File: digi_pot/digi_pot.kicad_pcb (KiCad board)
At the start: 2 copper layers, 30 x 30 mm, 22 parts, among them J1 Conn_01x08_Male, J2 Conn_01x06_Male, J3 Conn_01x03_Male, J4 Conn_01x03_Male, J5 Conn_01x06_Male, SW1 Rotary_Encoder, U1 ATmega328P-AU, U2 MCP42050

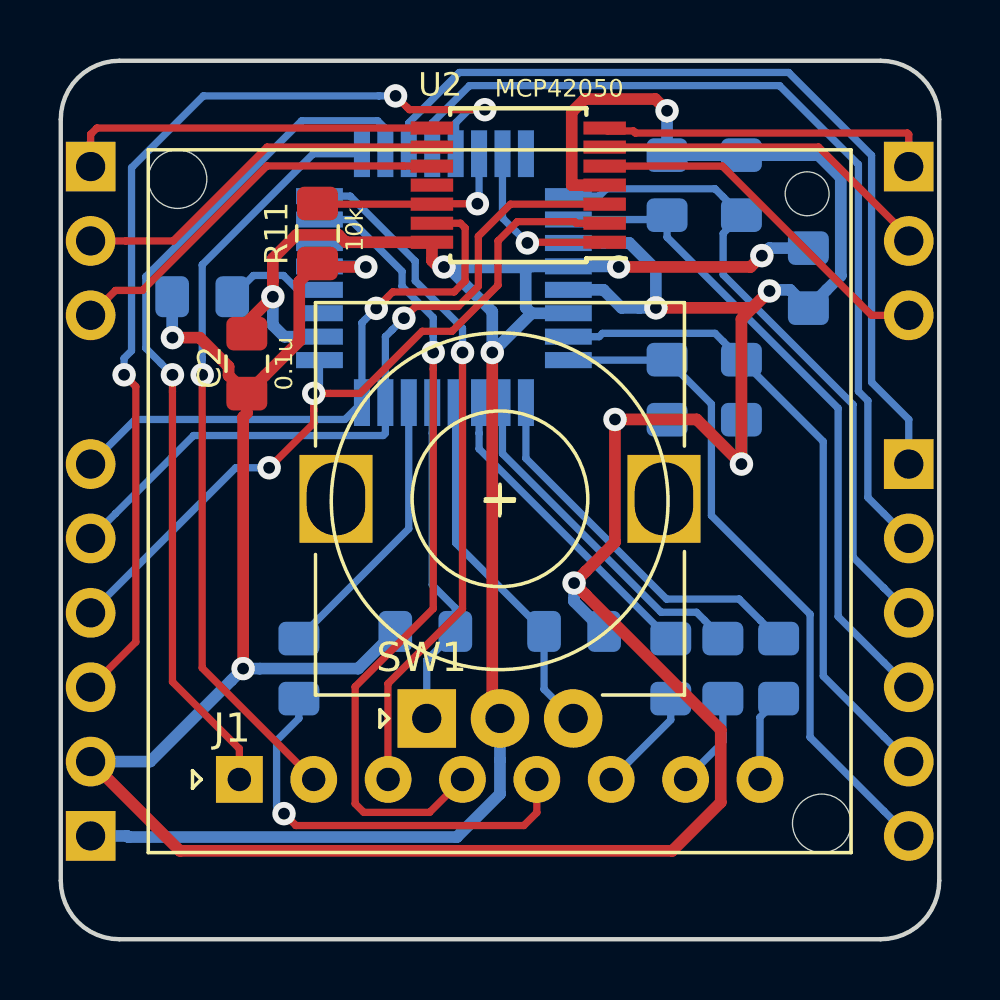
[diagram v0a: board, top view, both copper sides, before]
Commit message: Switching to AD5262 digital pot.
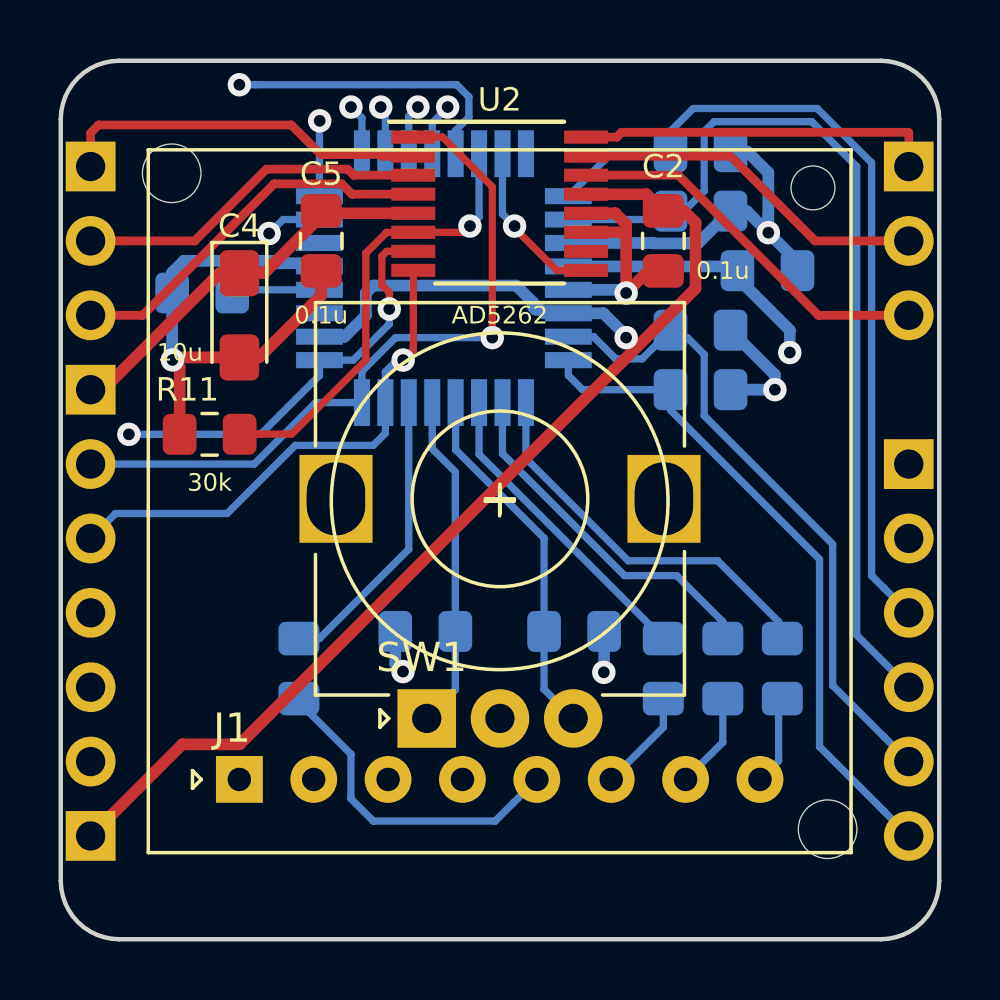
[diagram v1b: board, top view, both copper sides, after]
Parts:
- added C4: 10u, Capacitor_Tantalum_SMD:CP_EIA-3216-18_Kemet-A_Pad1.58x1.35mm_HandSolder, F.Cu at (139.7, 86.4)
- added C5: 0.1u, Capacitor_SMD:C_0805_2012Metric_Pad1.15x1.40mm_HandSolder, F.Cu at (142.5, 83.8)
- added J6: Conn_01x01_Male, Connector_PinHeader_2.54mm:PinHeader_1x01_P2.54mm_Vertical, B.Cu at (134.6, 88.9)
- R10, R11, R5, R6, R7, R8, R9: value 10k -> 30k
- U2: value MCP42050 -> AD5262; footprint Package_SO:TSSOP-14_4.4x5mm_P0.65mm -> Package_SO:TSSOP-16_4.4x5mm_P0.65mm
- moved C2 14.8 mm to (154.2, 83.8)
- moved R11 7.78 mm to (138.7, 90.4), turned to 0 degrees
- moved R9 2.47 mm to (155.4, 86.9), turned to 180 degrees
- moved R7 1.81 mm to (155.4, 80.8), turned to 180 degrees
- moved R8 1.45 mm to (155.4, 82.8), turned to 180 degrees
- moved C1 1.42 mm to (157.7, 84.8), turned to 0 degrees
- moved R10 1.14 mm to (155.4, 88.9), turned to 180 degrees
- moved U2 0.90 mm to (148.6, 82.5), turned to 0 degrees
- moved R2 0.25 mm to (154.2, 98.4)
- moved C3 0.13 mm to (138.4, 85.6)
- moved R4 0.13 mm to (158.2, 98.4)
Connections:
- U2 pad 1: MCP_CS -> MISO
- U2 pad 10: Net-(J3-Pad3) -> Net-(U2-Pad10)
- U2 pad 11: Net-(U2-Pad11) -> GND
- U2 pad 12: MCP_SHDN -> GND
- U2 pad 13: MISO -> +5V
- U2 pad 14: +5V -> Net-(J4-Pad3)
- U2 pad 2: SCK -> Net-(J3-Pad1)
- U2 pad 3: MOSI -> Net-(J3-Pad2)
- U2 pad 4: GND -> Net-(J3-Pad3)
- U2 pad 5: Net-(J4-Pad3) -> +9V
- U2 pad 6: Net-(J4-Pad2) -> MCP_SHDN
- U2 pad 7: Net-(J4-Pad1) -> SCK
- U2 pad 8: Net-(J3-Pad1) -> MOSI
- U2 pad 9: Net-(J3-Pad2) -> MCP_CS
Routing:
- net +5V: track 63.6 -> 105.3 mm, vias 5 -> 2
- net GND: track 124.6 -> 107.0 mm, vias 9 -> 6
- net +9V: track 0.00 -> 13.7 mm
- net A1: track 23.0 -> 31.6 mm
- net MCP_SHDN: track 7.21 -> 15.6 mm
- net MOSI: track 25.2 -> 17.6 mm
- net A0: track 22.9 -> 28.7 mm
- net SCL: track 30.7 -> 25.6 mm, vias 0 -> 1
- net SCK: track 25.8 -> 21.0 mm
- net MISO: track 20.0 -> 24.7 mm
- net SDA: track 29.8 -> 25.4 mm, vias 0 -> 1
- net Net-(J1-Pad5): track 14.8 -> 11.4 mm, vias 1 -> 0
- net LED3: track 23.6 -> 26.2 mm
- net LED2: track 26.4 -> 28.3 mm
- net RST: track 34.2 -> 32.8 mm, vias 3 -> 1
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- added copper zone on In1.Cu, net GND
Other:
- copper layers 2 -> 4
- net class Medium added: clearance 0.2, trace_width 0.3, via_dia 0.8, via_drill 0.4
- board text added: "+9V"
- board text added: "2020.02.12"
- board text removed: "2019.09.23"

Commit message: Using standard Atmega328 symbol.
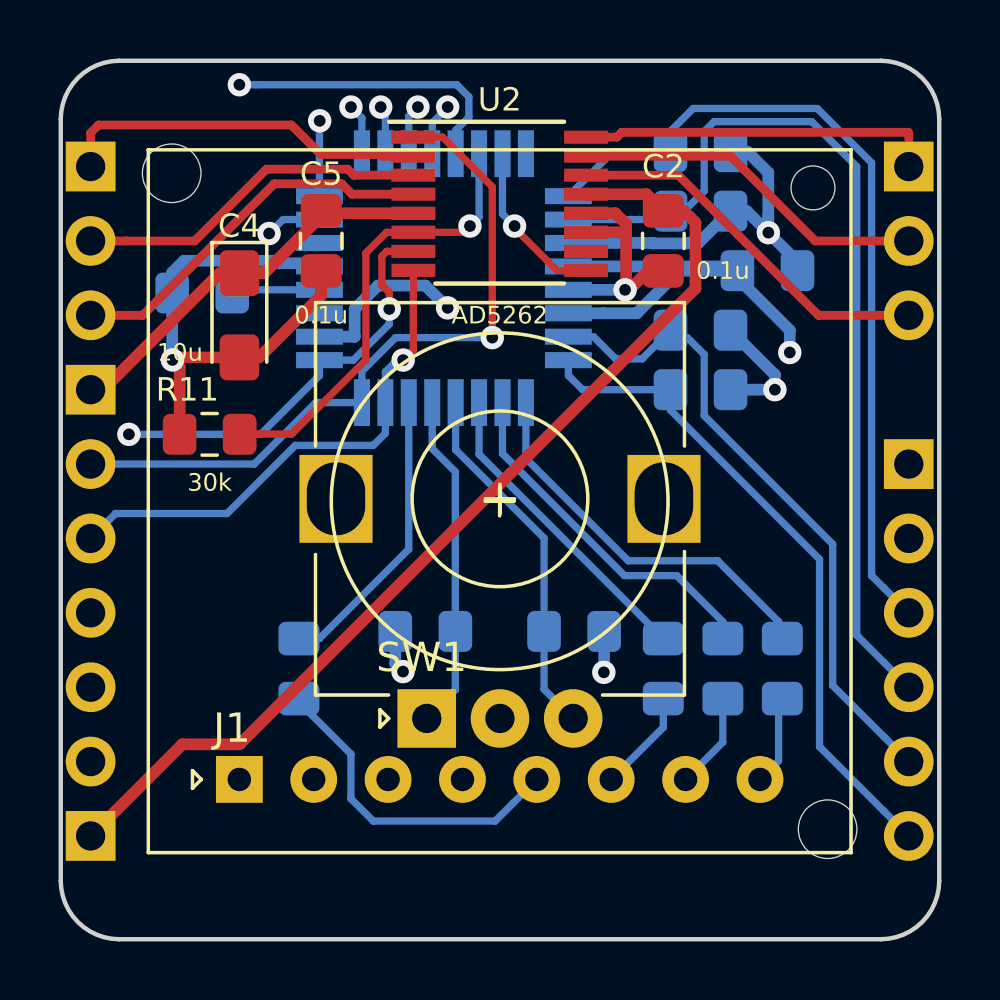
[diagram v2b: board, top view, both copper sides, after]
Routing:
- net +5V: track 105.3 -> 111.0 mm
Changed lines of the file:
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@@
     (thickness 1.6)
     (drawings 26)
-    (tracks 363)
+    (tracks 359)
     (zones 0)
     (modules 25)
@@
     (tags "QFP 0.8")
     (attr smd)
-    (fp_text reference U1 (at -0.127 5.842 180) (layer B.SilkS)
+    (fp_text reference U1 (at 0 6.05) (layer B.SilkS)
       (effects (font (size 0.8 0.8) (thickness 0.1)) (justify mirror))
     )
-    (fp_text value ATmega328P-AU (at -1.651 -5.842 180) (layer B.SilkS)
+    (fp_text value ATmega328P-AU (at 0 -6.05) (layer B.SilkS)
       (effects (font (size 0.6 0.6) (thickness 0.1)) (justify mirror))
     )
-    (fp_text user %R (at 0 0 180) (layer B.Fab)
+    (fp_text user %R (at 0 0) (layer B.Fab)
       (effects (font (size 1 1) (thickness 0.15)) (justify mirror))
     )
@@
   (segment (start 157.048 80.772) (end 157.763696 81.487696) (width 0.4) (layer B.Cu) (net 14))
   (segment (start 156.473 80.772) (end 157.048 80.772) (width 0.4) (layer B.Cu) (net 14))
-  (via (at 152.908 85.598) (size 0.8) (drill 0.4) (layers F.Cu B.Cu) (net 14))
   (segment (start 152.908 83.566) (end 152.908 85.598) (width 0.4) (layer F.Cu) (net 14))
   (segment (start 137.922 98.298) (end 140.773685 98.298) (width 0.4) (layer In1.Cu) (net 14))
-  (segment (start 152.8 85.49) (end 152.908 85.598) (width 0.4) (layer B.Cu) (net 14))
-  (segment (start 150.935 85.49) (end 152.8 85.49) (width 0.4) (layer B.Cu) (net 14))
   (segment (start 137.5005 87.7975) (end 137.414 87.884) (width 0.4) (layer F.Cu) (net 14))
   (segment (start 137.405 87.875) (end 137.414 87.884) (width 0.4) (layer B.Cu) (net 14))
@@
   (segment (start 141.002483 98.526798) (end 140.773685 98.298) (width 0.4) (layer In1.Cu) (net 14))
   (segment (start 145.288 98.526798) (end 141.002483 98.526798) (width 0.4) (layer In1.Cu) (net 14))
-  (segment (start 152.4 85.598) (end 152.908 85.598) (width 0.4) (layer In1.Cu) (net 14))
-  (segment (start 150.114 87.884) (end 152.4 85.598) (width 0.4) (layer In1.Cu) (net 14))
-  (segment (start 150.114 88.957685) (end 150.114 87.884) (width 0.4) (layer In1.Cu) (net 14))
-  (segment (start 140.773685 98.298) (end 150.114 88.957685) (width 0.4) (layer In1.Cu) (net 14))
   (segment (start 157.226 88.138) (end 157.988 88.9) (width 0.4) (layer In1.Cu) (net 14))
   (segment (start 157.226 84.074255) (end 157.226 88.138) (width 0.4) (layer In1.Cu) (net 14))
   (segment (start 157.763696 83.536559) (end 157.226 84.074255) (width 0.4) (layer In1.Cu) (net 14))
-  (segment (start 153.788 85.598) (end 152.908 85.598) (width 0.4) (layer In1.Cu) (net 14))
-  (segment (start 157.09 88.9) (end 153.788 85.598) (width 0.4) (layer In1.Cu) (net 14))
-  (segment (start 157.988 88.9) (end 157.09 88.9) (width 0.4) (layer In1.Cu) (net 14))
   (segment (start 145.770798 98.044) (end 145.288 98.526798) (width 0.4) (layer In1.Cu) (net 14))
   (segment (start 151.638 98.044) (end 145.770798 98.044) (width 0.4) (layer In1.Cu) (net 14))
@@
   (segment (start 156.473 86.868) (end 156.473 86.877) (width 0.4) (layer B.Cu) (net 14))
   (segment (start 156.473 88.9) (end 157.988 88.9) (width 0.4) (layer B.Cu) (net 14))
+  (via (at 152.870815 85.49) (size 0.8) (drill 0.4) (layers F.Cu B.Cu) (net 14))
+  (segment (start 150.935 85.49) (end 152.870815 85.49) (width 0.4) (layer B.Cu) (net 14))
+  (segment (start 153.788 85.598) (end 157.09 88.9) (width 0.4) (layer In1.Cu) (net 14))
+  (segment (start 152.4 85.598) (end 153.788 85.598) (width 0.4) (layer In1.Cu) (net 14))
+  (segment (start 157.09 88.9) (end 157.988 88.9) (width 0.4) (layer In1.Cu) (net 14))
+  (segment (start 150.114 87.884) (end 152.4 85.598) (width 0.4) (layer In1.Cu) (net 14))
+  (segment (start 150.114 89.535) (end 150.114 87.884) (width 0.4) (layer In1.Cu) (net 14))
+  (segment (start 141.351 98.298) (end 150.114 89.535) (width 0.4) (layer In1.Cu) (net 14))
+  (segment (start 140.773685 98.298) (end 141.351 98.298) (width 0.4) (layer In1.Cu) (net 14))
   (via (at 158.496 87.63) (size 0.8) (drill 0.4) (layers F.Cu B.Cu) (net 15))
   (segment (start 156.563 84.69) (end 156.709 84.836) (width 0.4) (layer B.Cu) (net 15))
@@
   (segment (start 152.4 104.14) (end 153.598401 102.941599) (width 0.4) (layer In2.Cu) (net 15))
   (segment (start 134.62 104.14) (end 152.4 104.14) (width 0.4) (layer In2.Cu) (net 15))
-  (segment (start 150.101002 86.29) (end 150.935 86.29) (width 0.4) (layer B.Cu) (net 15))
-  (segment (start 149.155002 85.344) (end 149.734999 85.923997) (width 0.4) (layer B.Cu) (net 15))
-  (segment (start 144.018 85.598) (end 144.272 85.344) (width 0.4) (layer B.Cu) (net 15))
-  (segment (start 144.018 86.367002) (end 144.018 85.598) (width 0.4) (layer B.Cu) (net 15))
-  (segment (start 143.295002 87.09) (end 144.018 86.367002) (width 0.4) (layer B.Cu) (net 15))
-  (segment (start 149.976003 86.165001) (end 150.101002 86.29) (width 0.4) (layer B.Cu) (net 15))
-  (segment (start 142.435 87.09) (end 143.295002 87.09) (width 0.4) (layer B.Cu) (net 15))
-  (segment (start 149.734999 86.085001) (end 149.814999 86.165001) (width 0.4) (layer B.Cu) (net 15))
-  (segment (start 149.814999 86.165001) (end 149.976003 86.165001) (width 0.4) (layer B.Cu) (net 15))
-  (segment (start 149.734999 85.923997) (end 149.734999 86.085001) (width 0.4) (layer B.Cu) (net 15))
-  (segment (start 144.272 85.344) (end 149.155002 85.344) (width 0.4) (layer B.Cu) (net 15))
-  (via (at 152.908 87.122) (size 0.8) (drill 0.4) (layers F.Cu B.Cu) (net 15))
-  (segment (start 152.908 87.063) (end 152.908 87.122) (width 0.4) (layer B.Cu) (net 15))
-  (segment (start 153.416 87.63) (end 152.908 87.122) (width 0.4) (layer In2.Cu) (net 15))
-  (segment (start 152.508001 87.521999) (end 152.908 87.122) (width 0.4) (layer In2.Cu) (net 15))
-  (segment (start 158.496 87.63) (end 153.416 87.63) (width 0.4) (layer In2.Cu) (net 15))
-  (segment (start 152.146 94.996) (end 152.146 87.884) (width 0.4) (layer In2.Cu) (net 15))
-  (segment (start 152.135 86.29) (end 152.908 87.063) (width 0.4) (layer B.Cu) (net 15))
-  (segment (start 152.146 87.884) (end 152.508001 87.521999) (width 0.4) (layer In2.Cu) (net 15))
-  (segment (start 150.935 86.29) (end 152.135 86.29) (width 0.4) (layer B.Cu) (net 15))
   (segment (start 153.608 82.225) (end 154.178 82.795) (width 0.4) (layer F.Cu) (net 15))
   (segment (start 151.54 82.225) (end 153.608 82.225) (width 0.4) (layer F.Cu) (net 15))
@@
   (segment (start 154.878 82.795) (end 155.27801 83.19501) (width 0.4) (layer F.Cu) (net 15))
   (segment (start 154.178 82.795) (end 154.878 82.795) (width 0.4) (layer F.Cu) (net 15))
+  (segment (start 153.416 87.63) (end 158.496 87.63) (width 0.4) (layer In2.Cu) (net 15))
+  (segment (start 152.146 88.9) (end 153.416 87.63) (width 0.4) (layer In2.Cu) (net 15))
+  (segment (start 152.146 94.996) (end 152.146 88.9) (width 0.4) (layer In2.Cu) (net 15))
+  (via (at 146.812 86.106) (size 0.8) (drill 0.4) (layers F.Cu B.Cu) (net 15))
+  (segment (start 146.812 86.782014) (end 146.812 86.106) (width 0.4) (layer In2.Cu) (net 15))
+  (segment (start 148.929986 88.9) (end 146.812 86.782014) (width 0.4) (layer In2.Cu) (net 15))
+  (segment (start 152.146 88.9) (end 148.929986 88.9) (width 0.4) (layer In2.Cu) (net 15))
+  (segment (start 143.635 87.09) (end 142.435 87.09) (width 0.4) (layer B.Cu) (net 15))
+  (segment (start 143.637 87.088) (end 143.635 87.09) (width 0.4) (layer B.Cu) (net 15))
+  (segment (start 143.637 86.141018) (end 143.637 87.088) (width 0.4) (layer B.Cu) (net 15))
+  (segment (start 144.434009 85.344009) (end 143.637 86.141018) (width 0.4) (layer B.Cu) (net 15))
+  (segment (start 146.050009 85.344009) (end 144.434009 85.344009) (width 0.4) (layer B.Cu) (net 15))
+  (segment (start 146.812 86.106) (end 146.050009 85.344009) (width 0.4) (layer B.Cu) (net 15))
+  (segment (start 153.273002 86.29) (end 152.135 86.29) (width 0.4) (layer B.Cu) (net 15))
+  (segment (start 154.727002 84.836) (end 153.273002 86.29) (width 0.4) (layer B.Cu) (net 15))
+  (segment (start 156.709 84.836) (end 154.727002 84.836) (width 0.4) (layer B.Cu) (net 15))
+  (segment (start 152.135 86.29) (end 150.935 86.29) (width 0.4) (layer B.Cu) (net 15))
   (segment (start 139.563 85.49) (end 139.455 85.598) (width 0.25) (layer B.Cu) (net 16))
   (segment (start 142.435 85.49) (end 139.563 85.49) (width 0.25) (layer B.Cu) (net 16))

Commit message: digi_pot: switch to KiCad 7.0
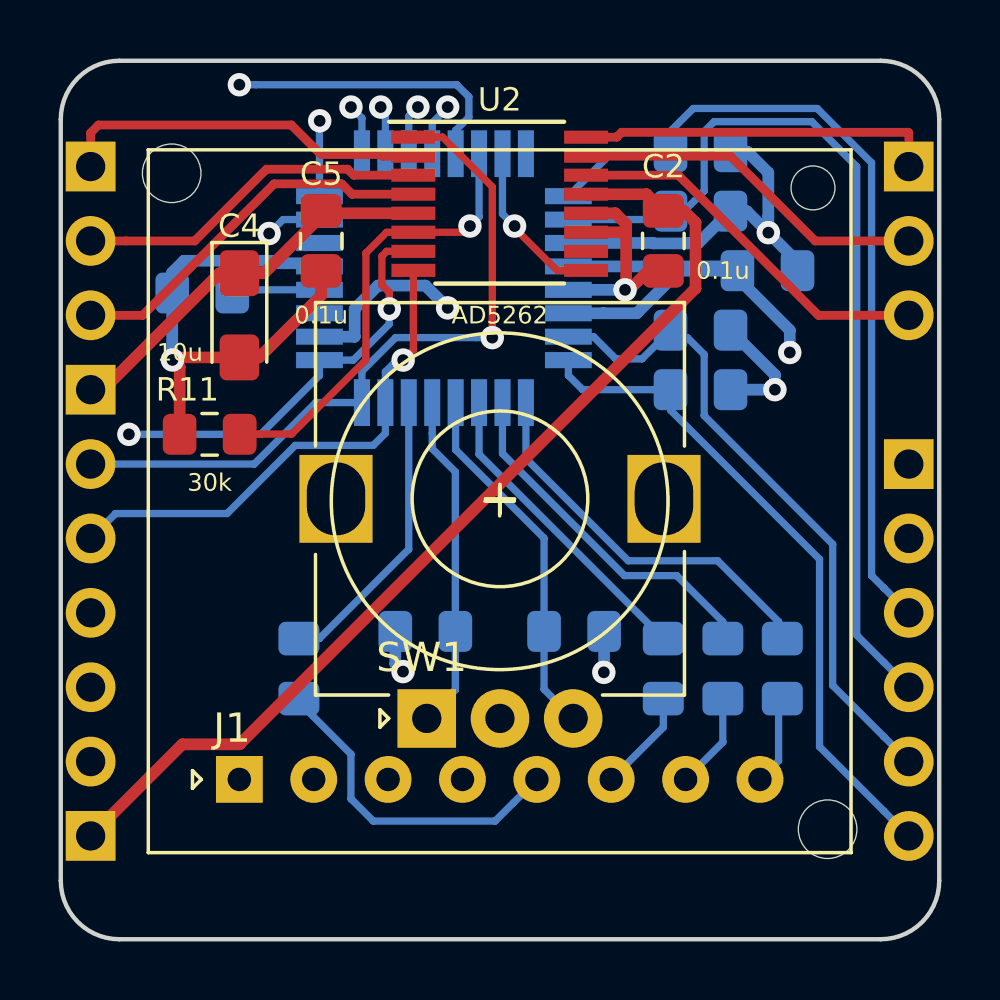
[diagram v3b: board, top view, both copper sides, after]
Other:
- net class Default removed
- net class Medium removed
- net class Thick removed
